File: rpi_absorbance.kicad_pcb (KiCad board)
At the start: 2 copper layers, 11.7 x 31.5 mm, 18 parts, among them P1 CONN_01X04, U1 LTC2461, U2 RPIABS_CONN, U3 SD100-13-23-222, U4 OPA381

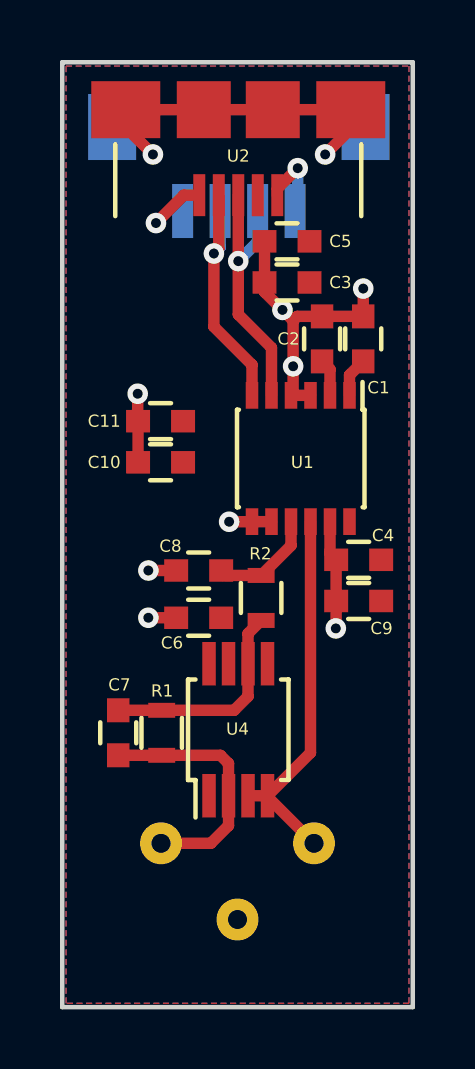
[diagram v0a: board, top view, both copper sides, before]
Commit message: Add I2C resistors and reorganize PCB
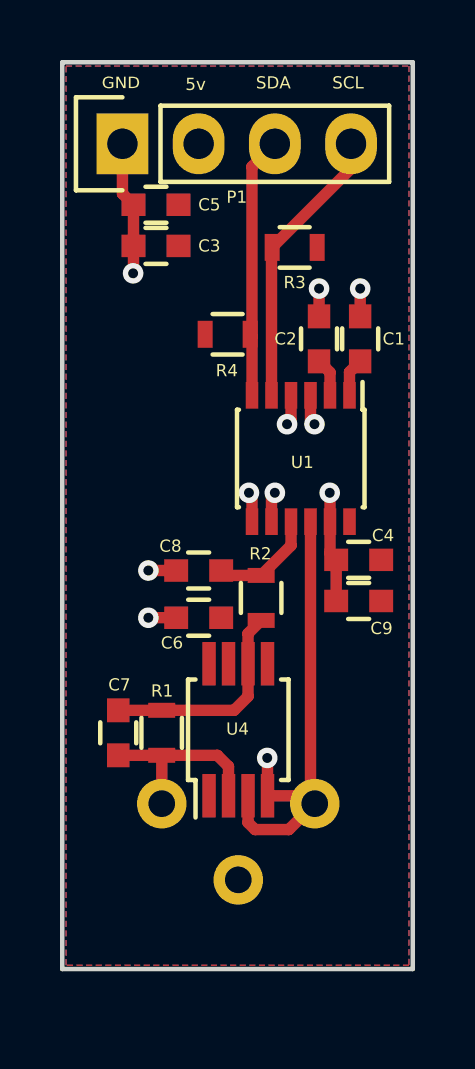
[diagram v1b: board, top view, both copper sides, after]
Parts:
- removed C10: 1u, Capacitors_SMD:C_0603
- removed C11: .1u, Capacitors_SMD:C_0603
- removed U2: RPIABS_CONN, footprints:FCI_10104111-0001LF
- added R3: 5k, Resistors_SMD:R_0603, F.Cu at (135.9, 89.6)
- added R4: 5k, Resistors_SMD:R_0603, F.Cu at (133.7, 92.5)
- P1: footprint footprints:Hirose_DF13-4P-1.25V(20) -> Pin_Headers:Pin_Header_Straight_1x04; moved to F.Cu
- moved P1 4.69 mm to (130.1, 86.2), turned to 90 degrees
- moved C3 4.54 mm to (131.3, 89.6)
- moved C5 4.54 mm to (131.3, 88.2)
- moved U3 1.32 mm to (134.0, 108.2)
- moved C1 0.10 mm to (138.1, 92.7)
- moved C2 0.10 mm to (136.7, 92.7)
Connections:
- P1 pad 2: /SDA -> VCC
- P1 pad 3: /SCL -> /SDA
- P1 pad 4: VCC -> /SCL
- U3 pad 2: GND -> Net-(U3-Pad2)
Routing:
- net GND: track 45.1 -> 32.2 mm
- net VCC: track 2.65 -> 0.00 mm, vias 1 -> 0
- net Net-(C7-Pad2): track 8.35 -> 6.42 mm
- net /SCL: track 9.07 -> 9.48 mm, vias 1 -> 0
- net /SDA: track 8.77 -> 8.70 mm, vias 1 -> 0
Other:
- board size 11.7 x 31.5 mm -> 11.7 x 30.2 mm
- board text added: "5v"
- board text added: "GND"
- board text added: "SCL"
- board text added: "SDA"

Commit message: Change footprints
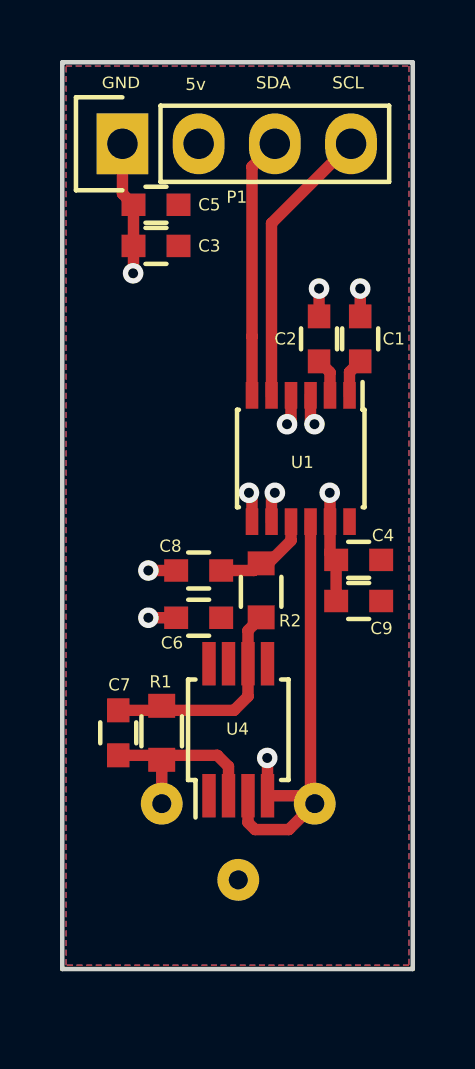
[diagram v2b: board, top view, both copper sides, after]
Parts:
- removed R3, R4: 5k, Resistors_SMD:R_0603
- R1, R2: footprint Resistors_SMD:R_0603 -> footprints:R_0603_smaller_handsolder
- U3: footprint footprints:TO-5 -> footprints:SD100-13-23-222
- moved R2 0.25 mm to (134.8, 101.0)
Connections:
- U3 pad 2: Net-(U3-Pad2) -> (no net)
- U4 pad 1: Net-(U4-Pad1) -> (no net)
- U4 pad 5: Net-(U4-Pad5) -> (no net)
- U4 pad 8: Net-(U4-Pad8) -> (no net)
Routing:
- net /SCL: track 9.48 -> 10.3 mm
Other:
- rule pad_to_mask_clearance: 0.0254 -> 0
